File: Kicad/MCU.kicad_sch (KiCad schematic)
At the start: 63 parts, among them J48 USB_C_Receptacle_USB2.0_16P, J50 Conn_ST_STDC14, SW1 SW_MEC_5E, U2 USBLC6-2P6, U3 STM32H573IITxQ

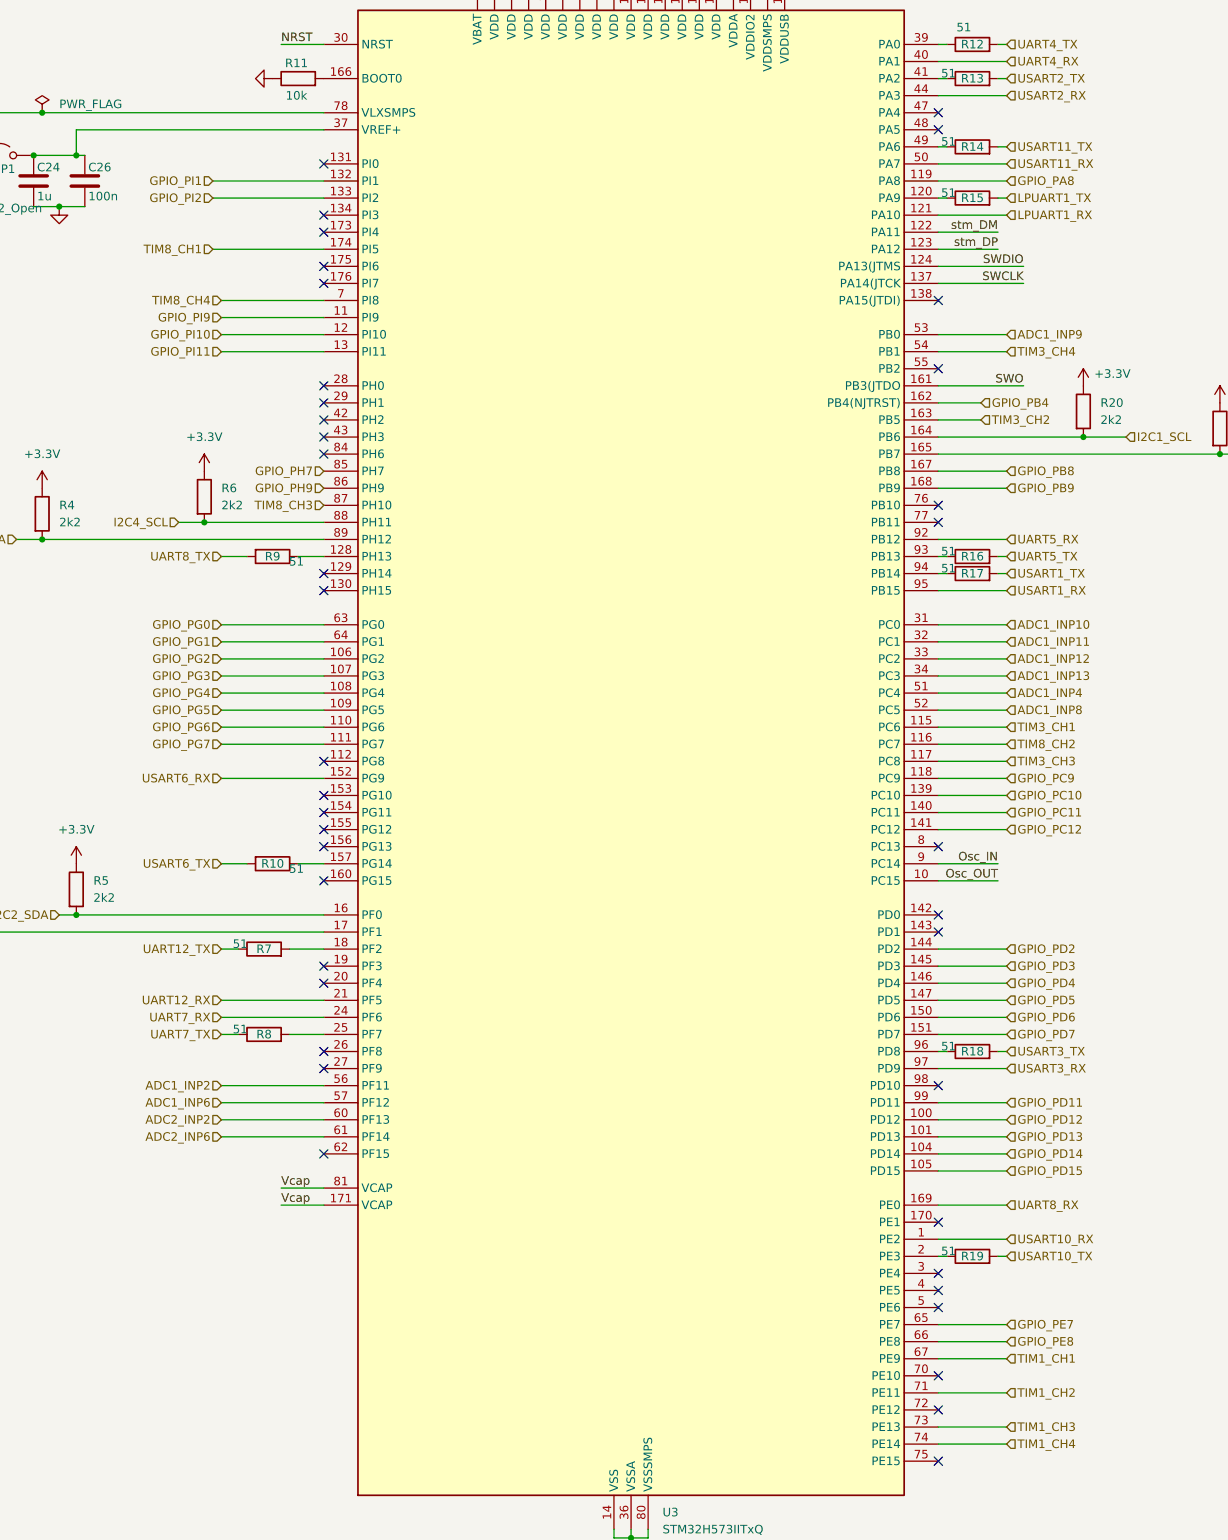
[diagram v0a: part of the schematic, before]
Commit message: ajout spi et maj readme
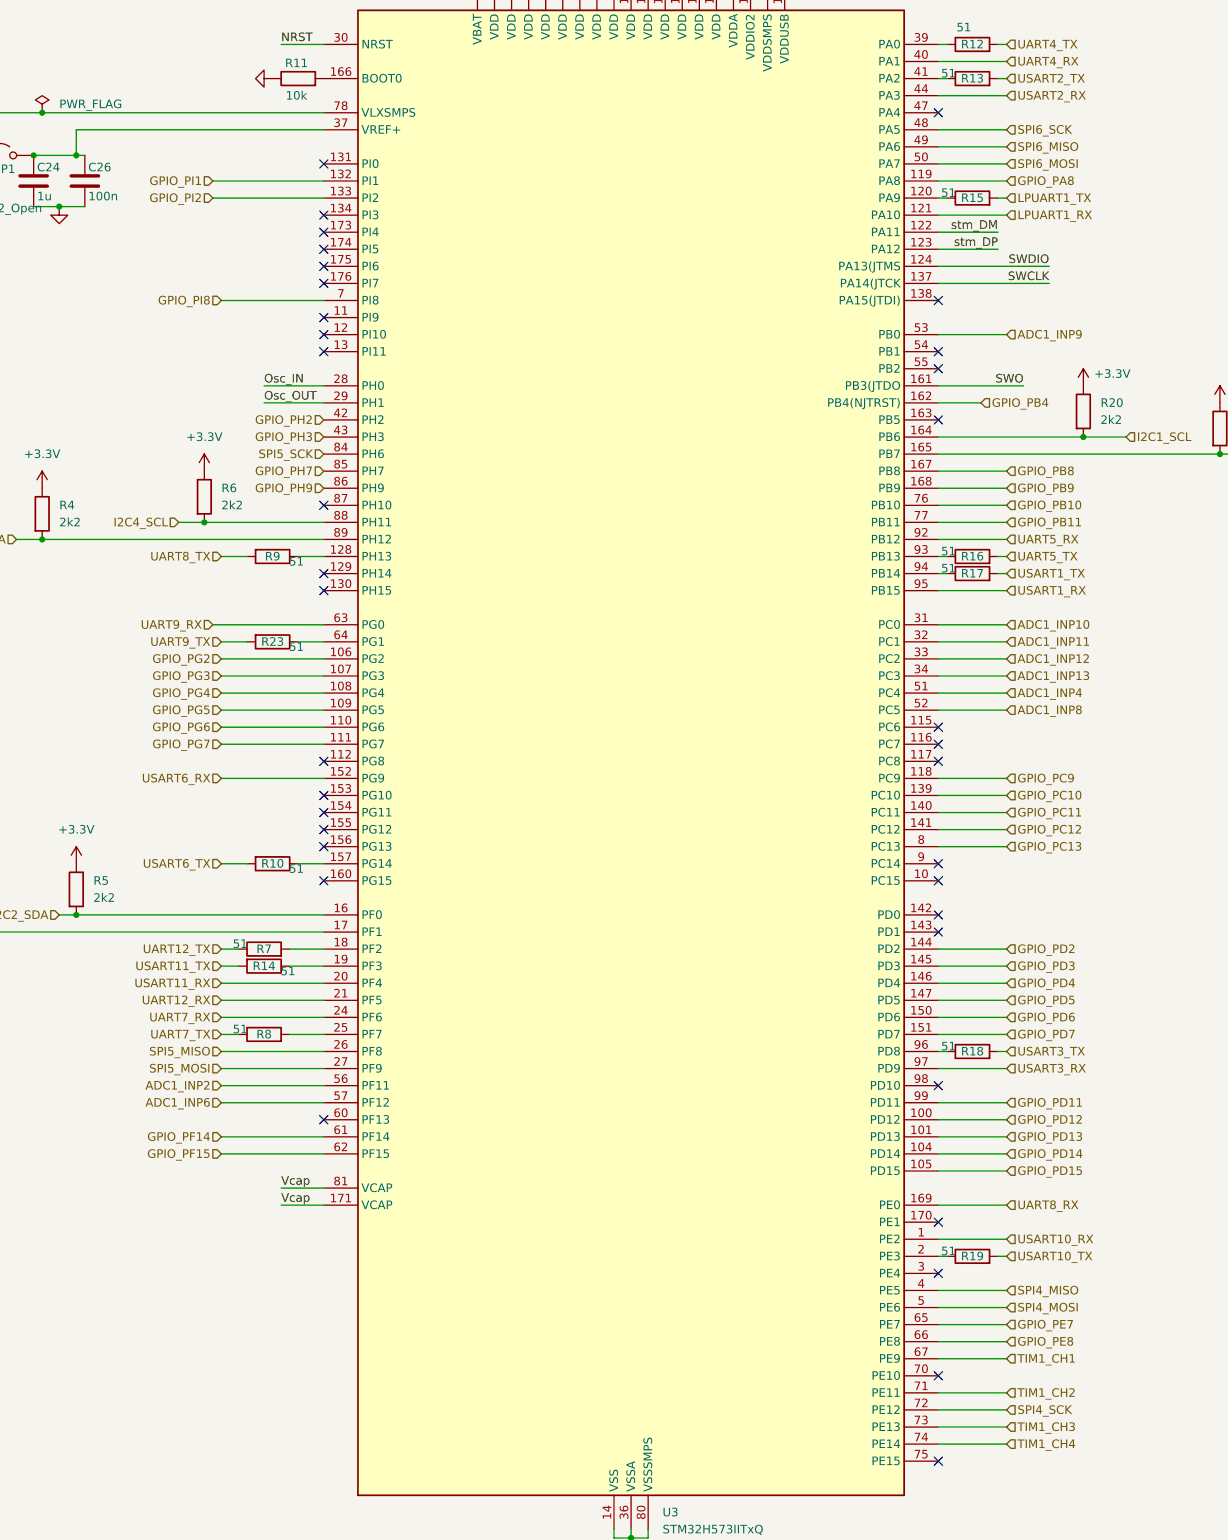
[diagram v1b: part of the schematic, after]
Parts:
- added R23: 51, Resistor_SMD:R_0402_1005Metric, symbol Device:R
- JP1: footprint TestPoint:TestPoint_2Pads_Pitch2.54mm_Drill0.8mm -> Connector_PinHeader_2.54mm:PinHeader_1x02_P2.54mm_Vertical
- SW1: footprint BoutonSMD:wurth_pushButton_SMD -> Switch:WS-TASU SMT Tact Switch 4.7x3.5 mm side push
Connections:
- net Osc_IN: now also U3.28 (PH0); no longer U3.9 (PC14)
- net Osc_OUT: now also U3.29 (PH1); no longer U3.10 (PC15)
- net USART11_RX: now also U3.20 (PF4); no longer U3.50 (PA7)
- net at R14.1: now also U3.19 (PF3); no longer U3.49 (PA6)
- net SPI5_MISO: now reaches U3.26 (PF8)
- net SPI5_MOSI: now reaches U3.27 (PF9)
- net SPI4_MISO: now reaches U3.4 (PE5)
- net GPIO_PH2: now reaches U3.42 (PH2)
- net GPIO_PH3: now reaches U3.43 (PH3)
- net SPI6_SCK: now reaches U3.48 (PA5)
- net SPI4_MOSI: now reaches U3.5 (PE6)
- net GPIO_PF15: now reaches U3.62 (PF15)
- net SPI4_SCK: now reaches U3.72 (PE12)
- net GPIO_PB10: now reaches U3.76 (PB10)
- net GPIO_PB11: now reaches U3.77 (PB11)
- net GPIO_PC13: now reaches U3.8 (PC13)
- net SPI5_SCK: now reaches U3.84 (PH6)
- net ADC2_INP2: no longer names the net of U3.60 (PF13)
- net ADC2_INP6 renamed GPIO_PF14
- net GPIO_PG0 renamed UART9_RX
- net GPIO_PG1: no longer names the net of U3.64 (PG1)
- net GPIO_PG1: now also R23.1
- net GPIO_PI10: no longer names the net of U3.12 (PI10)
- net GPIO_PI11: no longer names the net of U3.13 (PI11)
- net GPIO_PI9: no longer names the net of U3.11 (PI9)
- net TIM3_CH1: no longer names the net of U3.115 (PC6)
- net TIM3_CH2: no longer names the net of U3.163 (PB5)
- net TIM3_CH3: no longer names the net of U3.117 (PC8)
- net TIM3_CH4: no longer names the net of U3.54 (PB1)
- net TIM8_CH1: no longer names the net of U3.174 (PI5)
- net TIM8_CH2: no longer names the net of U3.116 (PC7)
- net TIM8_CH3: no longer names the net of U3.87 (PH10)
- net TIM8_CH4 renamed GPIO_PI8
- new net SPI6_MISO: U3.49 (PA6)
- new net SPI6_MOSI: U3.50 (PA7)
- new net UART9_TX: R23.2
- no-connect marks 46 -> 42
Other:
- moved on the sheet: R14

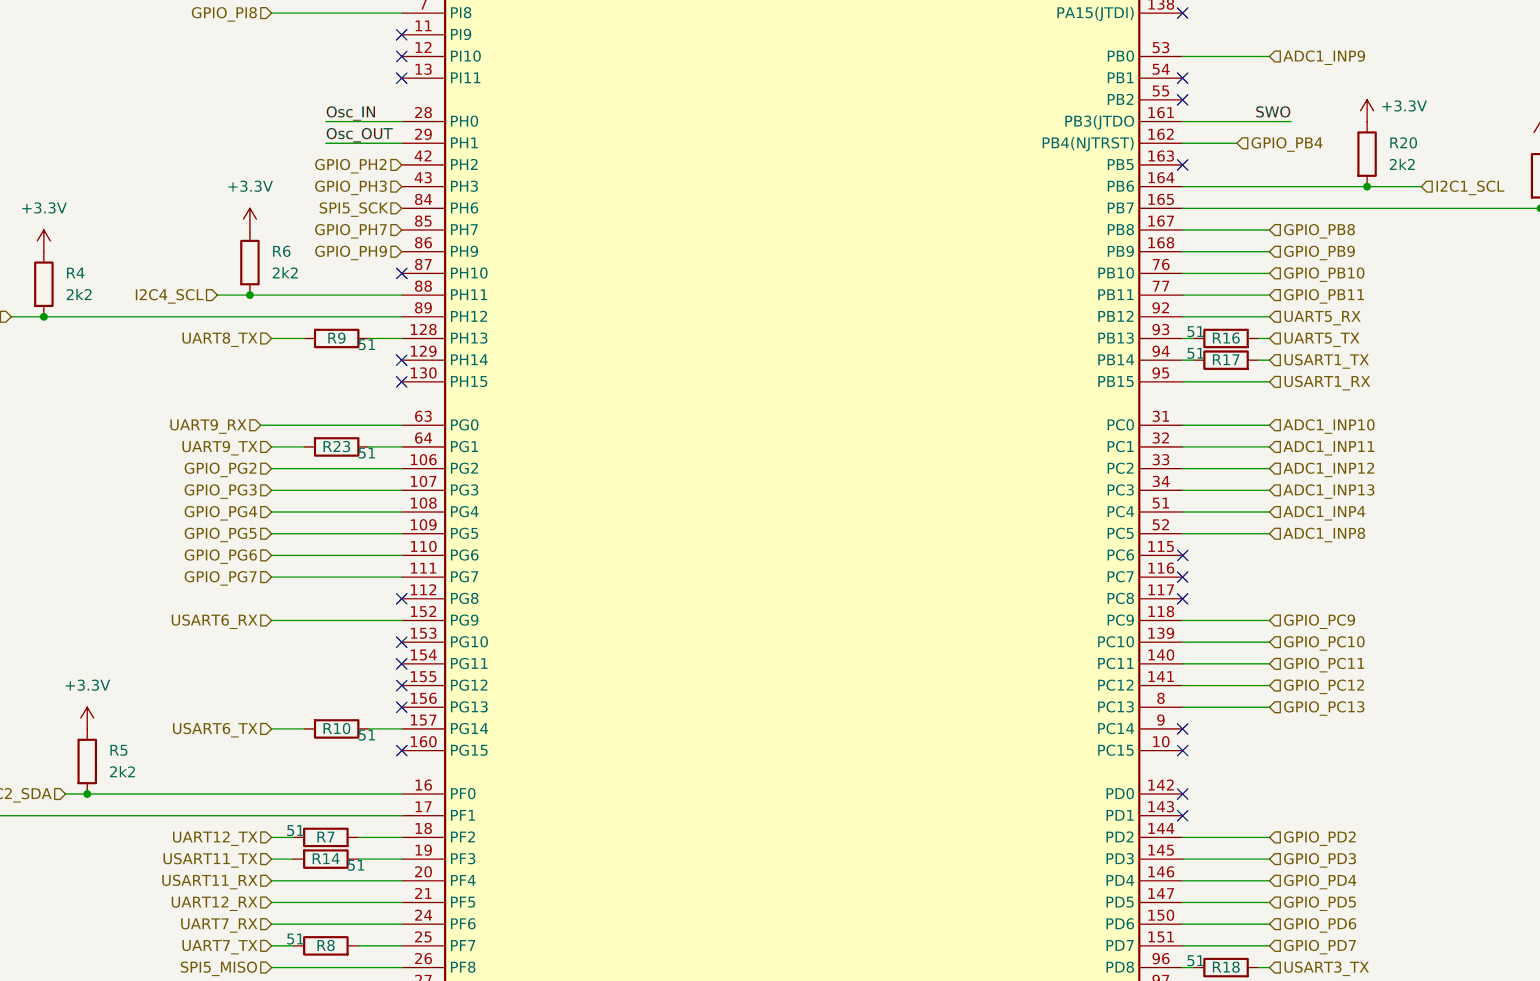
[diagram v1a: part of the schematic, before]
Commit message: ajout d'un connecteur SPI
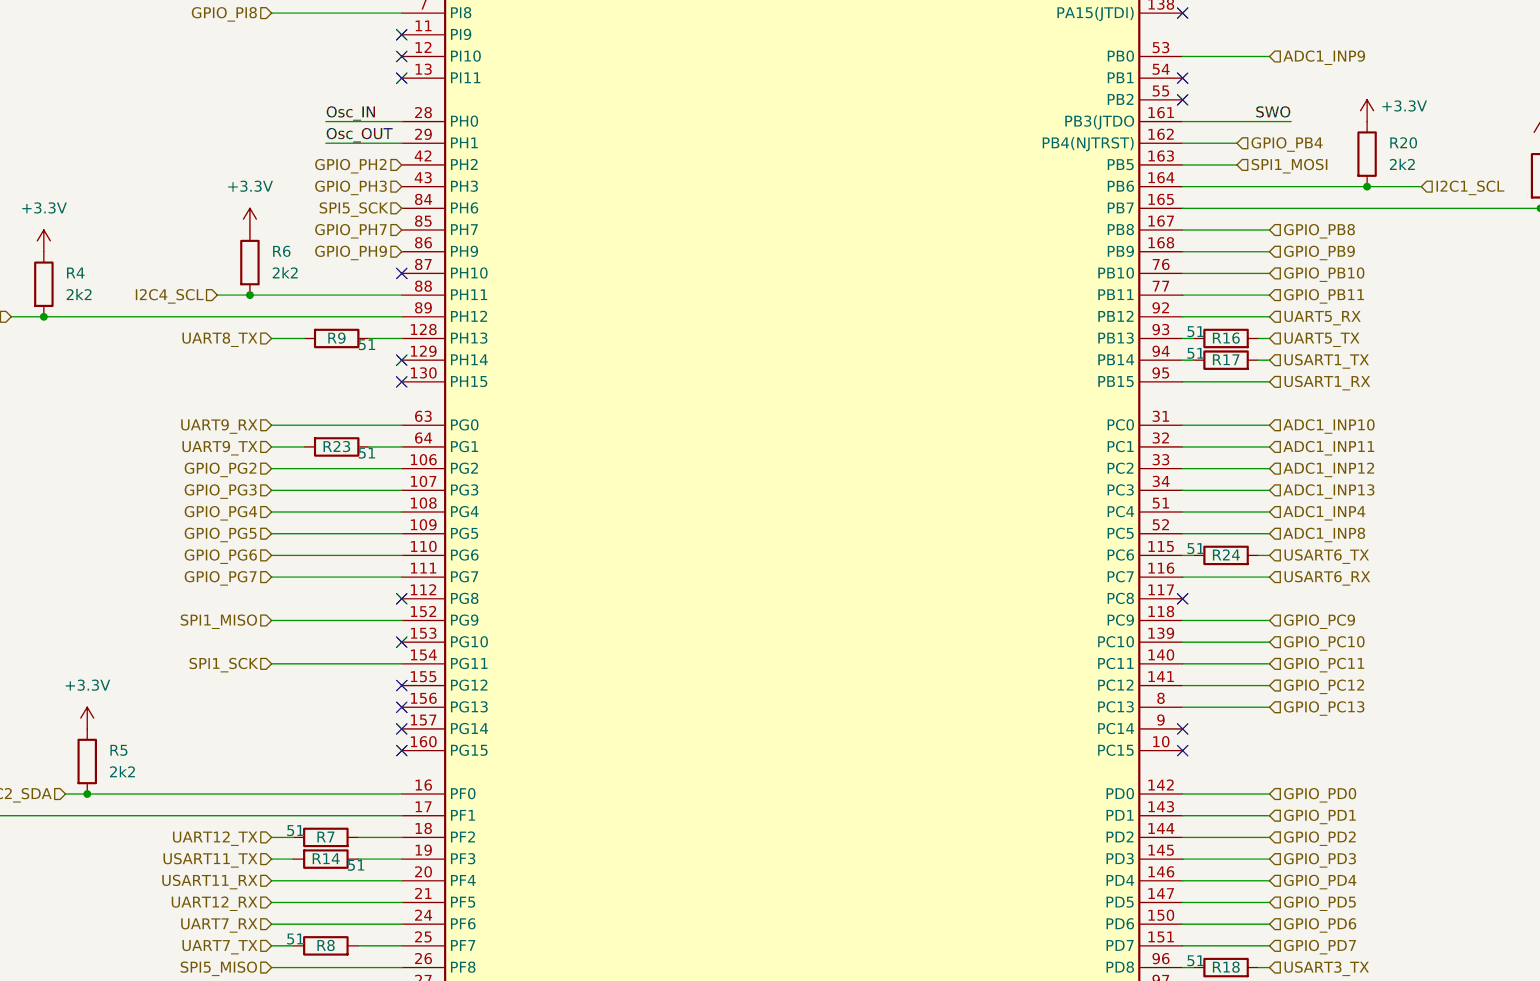
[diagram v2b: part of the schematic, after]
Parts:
- removed R10: 51, Resistor_SMD:R_0402_1005Metric, symbol Device:R
- added R24: 51, Resistor_SMD:R_0402_1005Metric, symbol Device:R
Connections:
- net USART6_RX: now also U3.116 (PC7); no longer U3.152 (PG9)
- net USART6_TX: now also R24.2
- net at U3.115 (PC6): now also R24.1
- net GPIO_PD0: now reaches U3.142 (PD0)
- net GPIO_PD1: now reaches U3.143 (PD1)
- net SPI1_SCK: now reaches U3.154 (PG11)
- net SPI1_MOSI: now reaches U3.163 (PB5)
- new net SPI1_MISO: U3.152 (PG9)
- no-connect marks 42 -> 37
